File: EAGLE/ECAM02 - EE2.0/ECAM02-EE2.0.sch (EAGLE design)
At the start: 50 parts, among them J1 MODULAR TOOL, J2 SPI, J3 MOT, J4 FTDI, J5 S4B-PH-SM4, J6 S5B-PH-SM, J7 RINGLIGHT, Q2 16MHz, U1 SP3485, U2 ATMEGA238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

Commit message: Component placement begun
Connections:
- removed net O_OUT: U2.PD2
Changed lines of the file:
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@@
-</segment>
-</net>
-<net name="O_OUT" class="0">
-<segment>
-<pinref part="U2" gate="G$1" pin="PD2"/>
-<wire x1="340.36" y1="220.98" x2="347.98" y2="220.98" width="0.1524" layer="91"/>
-<label x="342.9" y="220.98" size="1.778" layer="95" ratio="12"/>
 </segment>
 </net>

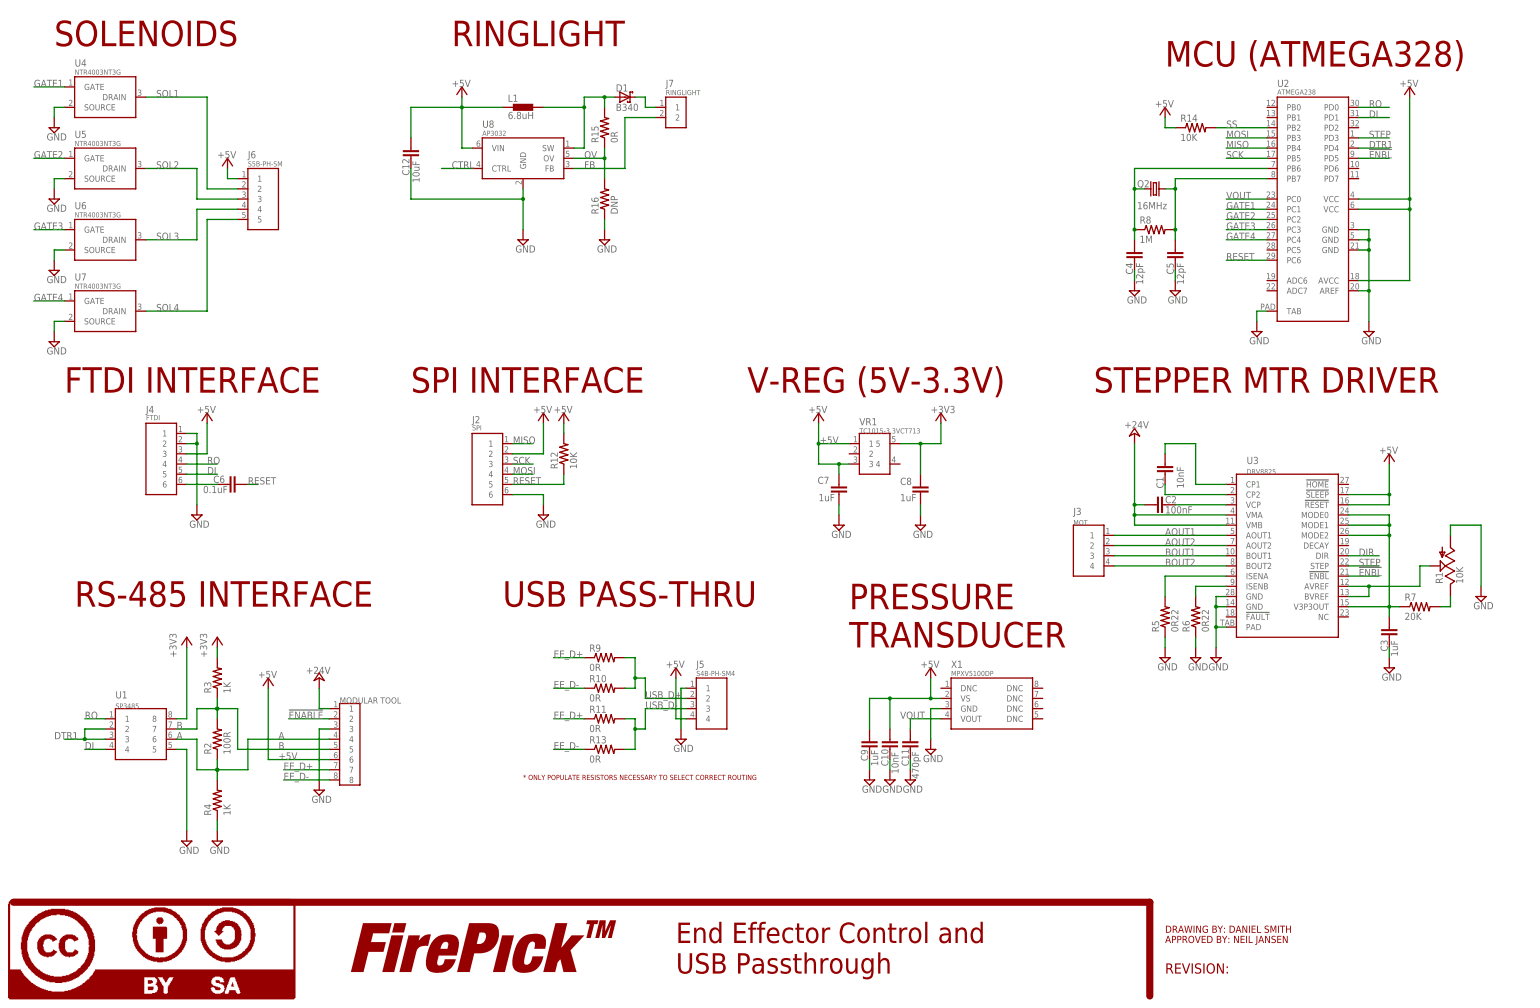
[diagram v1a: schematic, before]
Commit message: Finalized schematics (minus potential LDO regulator) for all boards. Layout partially done for EFD01
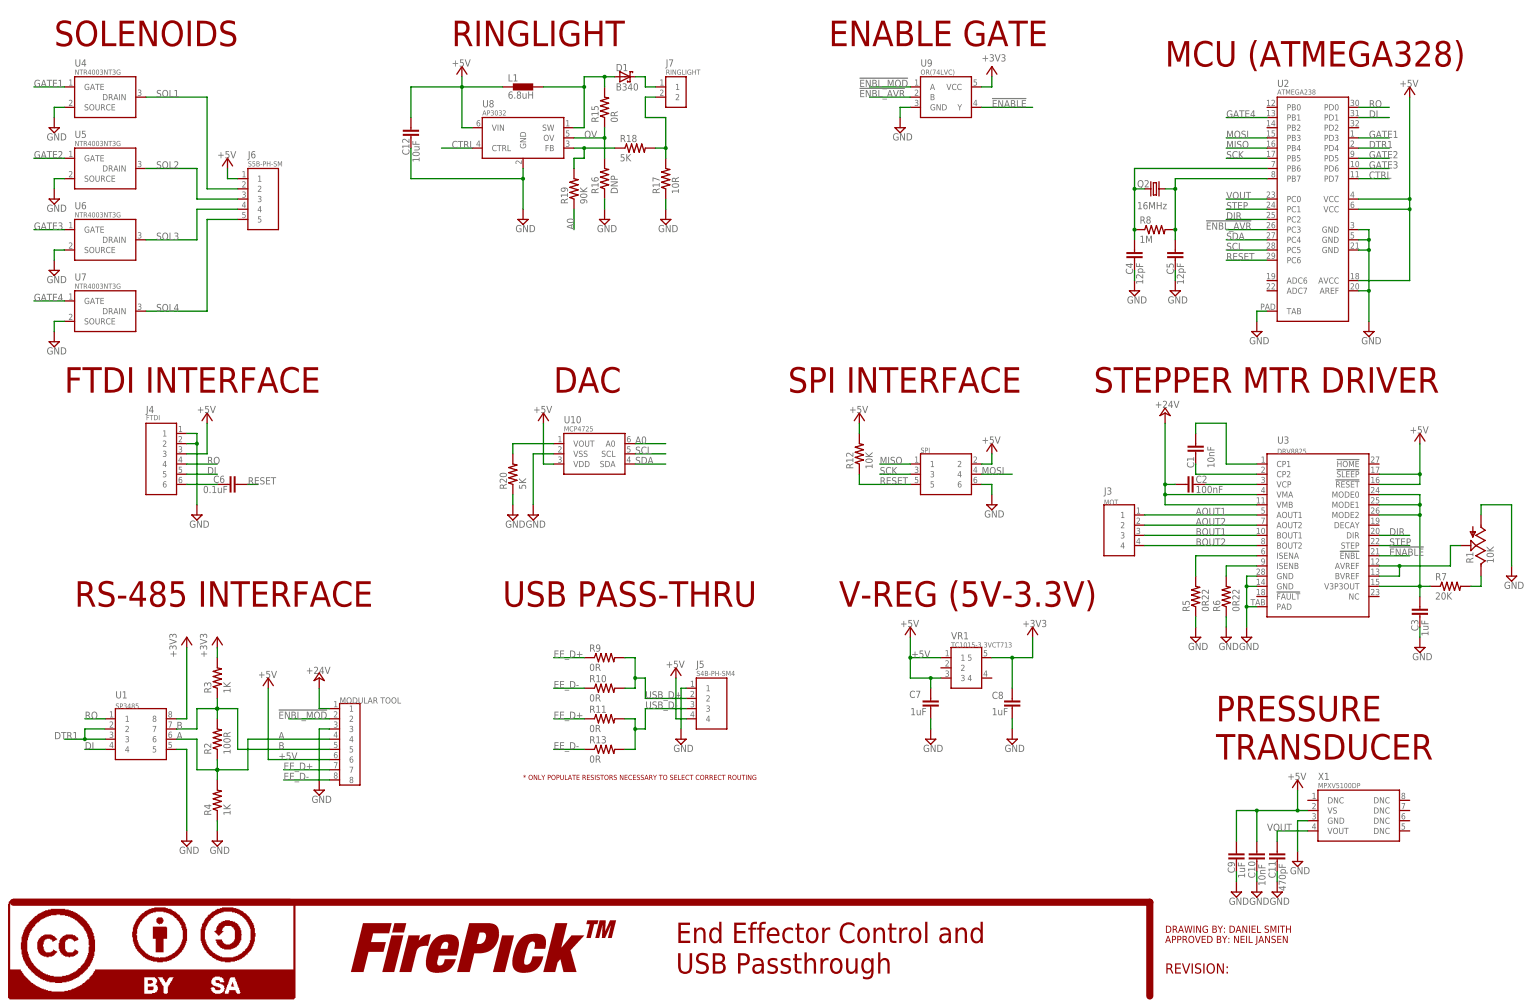
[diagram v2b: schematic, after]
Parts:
- removed R14: 10K, TinWhiskers:CPL-RES-0603-10K-0.1W
- added R17: 10R, TinWhiskers:CPL-RES-0603-10.0-0.1W
- added R18, R20: 5K, TinWhiskers:CPL-RES-0603-5K-0.1W
- added R19: 90K, TinWhiskers:CPL-RES-0603-90K-0.1W
- added U10: MCP4725, TinWhiskers:CPL-DAC-12BIT-SOT23
- added U9: OR(74LVC), TinWhiskers:CPL-IC-LOGIC-OR-1CH-74LVC
- J2: device TinWhiskers:CPL-CON-HEADER-0.1IN-6P-M -> TinWhiskers:CPL-CON-HEADER-0.1IN-2X3P-M; PARTNO 67996-206HLF -> (none)
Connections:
- removed net !ENBL: U2.PD5, U3.!ENBL
- removed net FB: J7.2, U8.FB
- removed net SS: R14.2, U2.PB2
- new net !ENBL_AVR: U2.PC3, U9.B
- new net !ENBL_MOD: J1.2, U9.A
- new net A0: R19.1, U10.A0
- new net N$10: R20.2, U10.VOUT
- new net N$3: J7.2, R17.2, R18.2
- new net N$4: R18.1, R19.2, U8.FB
- new net SCL: U10.SCL, U2.PC5
- new net SDA: U10.SDA, U2.PC4
- net !ENABLE: now also U3.!ENBL, U9.Y; no longer J1.2
- net +3V3: now also U9.VCC
- net +5V: now also U10.VDD; no longer R14.1
- net CTRL: now also U2.PD7
- net DIR: now also U2.PC2
- net GATE1: now also U2.PD3; no longer U2.PC1
- net GATE2: now also U2.PD5; no longer U2.PC2
- net GATE3: now also U2.PD6; no longer U2.PC3
- net GATE4: now also U2.PB1; no longer U2.PC4
- net GND: now also R17.1, R20.1, U10.VSS, U9.GND
- net STEP: now also U2.PC1; no longer U2.PD3
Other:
- note added: "DAC"
- note added: "ENABLE GATE"
- note added: "SPI"
- moved on the sheet: C1, C10, C11, C12, C2, C3, C7, C8, C9, D1, J3, J7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

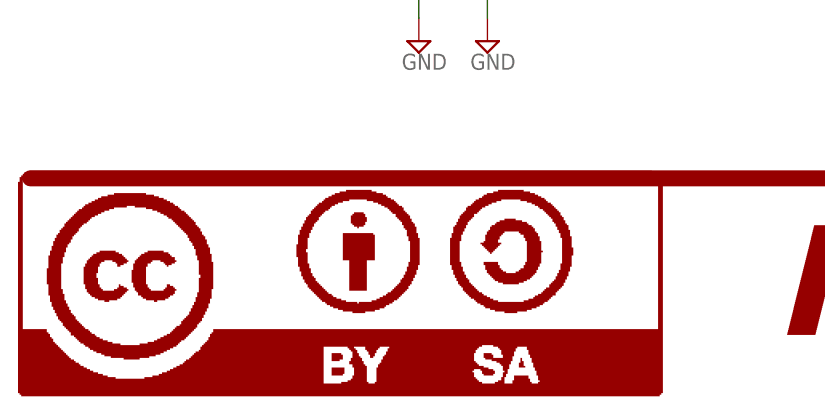
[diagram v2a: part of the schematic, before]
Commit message: Routed all boards. EFP01 has a serious problem with spacing. Even on minimum allowable there are 300 DRC errors.
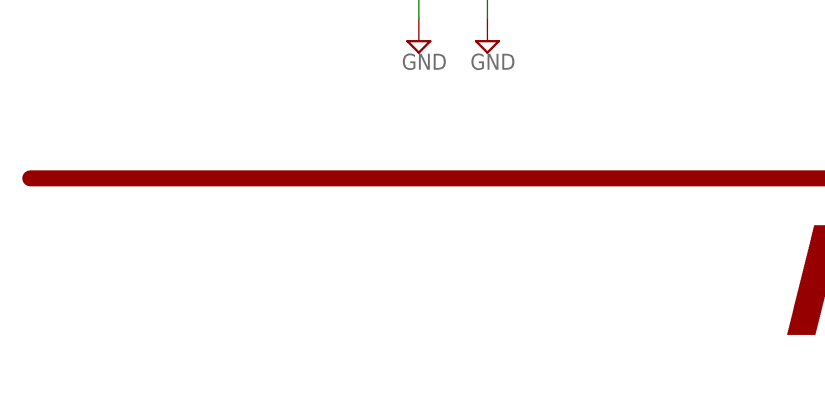
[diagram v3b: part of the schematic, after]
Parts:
- removed LOGO1: LOGO-CC-BY-SALARGE, FirePick:LOGO-CC-BY-SALARGE
- J1: device TinWhiskers:CPL-CON-JST-2.0MM-8P-M-RA -> TinWhiskers:CPL-CON-JST-2.0MM-8P-SMT-VRT
- J3: device TinWhiskers:CPL-CON-JST-2.0MM-4P-M-RA -> TinWhiskers:CPL-CON-HEADER-0.1IN-4P-M
- J4: device TinWhiskers:CPL-CON-JST-2.0MM-6P-M-RA -> TinWhiskers:CPL-CON-JST-2.0MM-6P-SMT-VRT
- J5: device TinWhiskers:CPL-CON-JST-2.0MM-4P-M-SMT-RA -> TinWhiskers:CPL-CON-JST-2.0MM-4P-M-SMT-VRT
- J6: device TinWhiskers:CPL-CON-JST-2.0MM-5P-M-SMT-RA -> TinWhiskers:CPL-CON-JST-2.0MM-5P-SMT-VRT
- J7: device TinWhiskers:CPL-CON-JST-2.0MM-2P-M-SMT-RA -> TinWhiskers:CPL-CON-JST-2.0MM-2P-M-SMT-VRT
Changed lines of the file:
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@@
 <parts>
 <part name="FRAME1" library="TinWhiskers" deviceset="A3L-LOC" device=""/>
-<part name="LOGO1" library="FirePick" deviceset="LOGO-CC-BY-SA" device="LARGE"/>
 <part name="LOGO2" library="FirePick" deviceset="LOGO-FIREPICK" device="LARGE"/>
 <part name="U1" library="TinWhiskers" deviceset="SP3485" device="">
@@
 <part name="P+3" library="supply1" deviceset="+5V" device=""/>
 <part name="+3V1" library="supply1" deviceset="+3V3" device=""/>
-<part name="J4" library="TinWhiskers" deviceset="CPL-CON-JST-2.0MM-6P-M-RA" device="" value="FTDI">
+<part name="J4" library="TinWhiskers" deviceset="CPL-CON-JST-2.0MM-6P-SMT-VRT" device="" value="FTDI">
 <attribute name="PARTNO" value="S6B-PH-SM4-TB(LF)(SN)"/>
 </part>
@@
 </part>
 <part name="SUPPLY8" library="TinWhiskers" deviceset="GND" device=""/>
-<part name="J3" library="TinWhiskers" deviceset="CPL-CON-JST-2.0MM-4P-M-RA" device="" value="MOT">
+<part name="J3" library="TinWhiskers" deviceset="CPL-CON-HEADER-0.1IN-4P-M" device="" value="MOT">
 <attribute name="PARTNO" value="S4B-PH-SM4-TB(LF)(SN)"/>
 </part>
 <part name="SUPPLY13" library="TinWhiskers" deviceset="GND" device=""/>
-<part name="J1" library="TinWhiskers" deviceset="CPL-CON-JST-2.0MM-8P-M-RA" device="" value="MODULAR TOOL">
+<part name="J1" library="TinWhiskers" deviceset="CPL-CON-JST-2.0MM-8P-SMT-VRT" device="" value="MODULAR TOOL">
 <attribute name="PARTNO" value="S8B-PH-SM4-TB(LF)(SN)"/>
 </part>
-<part name="J5" library="TinWhiskers" deviceset="CPL-CON-JST-2.0MM-4P-M-SMT-RA" device="" value="S4B-PH-SM4">
+<part name="J5" library="TinWhiskers" deviceset="CPL-CON-JST-2.0MM-4P-M-SMT-VRT" device="" value="S4B-PH-SM4">
 <attribute name="PARTNO" value="S4B-PH-SM4-TB(LF)(SN)"/>
 </part>
@@
 <part name="SUPPLY24" library="TinWhiskers" deviceset="GND" device=""/>
 <part name="SUPPLY25" library="TinWhiskers" deviceset="GND" device=""/>
-<part name="J6" library="TinWhiskers" deviceset="CPL-CON-JST-2.0MM-5P-M-SMT-RA" device="" value="S5B-PH-SM"/>
+<part name="J6" library="TinWhiskers" deviceset="CPL-CON-JST-2.0MM-5P-SMT-VRT" device="" value="S5B-PH-SM"/>
 <part name="P+13" library="supply1" deviceset="+5V" device=""/>
 <part name="D1" library="TinWhiskers" deviceset="CPL-DIO-B340-13-F-SMA" device="" value="B340"/>
@@
 <part name="R16" library="TinWhiskers" deviceset="CPL-RES-0603-0-0.1W" device="" value="DNP"/>
 <part name="SUPPLY26" library="TinWhiskers" deviceset="GND" device=""/>
-<part name="J7" library="TinWhiskers" deviceset="CPL-CON-JST-2.0MM-2P-M-SMT-RA" device="" value="RINGLIGHT"/>
+<part name="J7" library="TinWhiskers" deviceset="CPL-CON-JST-2.0MM-2P-M-SMT-VRT" device="" value="RINGLIGHT"/>
 <part name="U9" library="TinWhiskers" deviceset="CPL-IC-LOGIC-OR-1CH-74LVC" device="" value="OR(74LVC)"/>
 <part name="SUPPLY28" library="TinWhiskers" deviceset="GND" device=""/>
@@
 <instances>
 <instance part="FRAME1" gate="G$1" x="0" y="0"/>
-<instance part="LOGO1" gate="G$1" x="3.81" y="3.81"/>
 <instance part="LOGO2" gate="G$1" x="88.9" y="10.16"/>
 <instance part="U1" gate="G$1" x="33.02" y="68.58" smashed="yes">

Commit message: Updated all boards to include changes for production
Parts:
- added C13, C14, C15, C16: 0.1uF, TinWhiskers:CPL-CAP-X7R-0603-0.1UF-35V
- added C17: 100uF, TinWhiskers:CPL-CAP-ALU-SMD-100UF-50V
- added C18: 10uF, TinWhiskers:CPL-CAP-ALU-6.4MM-10UF-10V
- added U11: NTR4003NT3G, TinWhiskers:CPL-MOSFET-NCH-SOT23
- J3: device TinWhiskers:CPL-CON-HEADER-0.1IN-4P-M -> TinWhiskers:CPL-CON-JST-2.0MM-4P-M-THRU-VRT
- J4: device TinWhiskers:CPL-CON-JST-2.0MM-6P-SMT-VRT -> TinWhiskers:CPL-CON-HEADER-0.1IN-6P-M
- J6: value S5B-PH-SM -> SOL+PUMP; device TinWhiskers:CPL-CON-JST-2.0MM-5P-SMT-VRT -> TinWhiskers:CPL-CON-JST-2.0MM-7P-M-SMT-VRT
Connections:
- new net N$12: J6.7, U11.DRAIN
- new net PUMP: U11.GATE, U2.PD2
- net +24V: now also C17.NEG, J6.1
- net +3V3: now also C14.2, C16.2
- net +5V: now also C13.2, C15.2, C18.NEG, J6.2; no longer J6.1
- net GND: now also C13.1, C14.1, C15.1, C16.1, C17.POS, C18.POS, U11.SOURCE; no longer U2.TAB
- net SOL1: now also J6.3; no longer J6.2
- net SOL2: now also J6.4; no longer J6.3
- net SOL3: now also J6.5; no longer J6.4
- net SOL4: now also J6.6; no longer J6.5

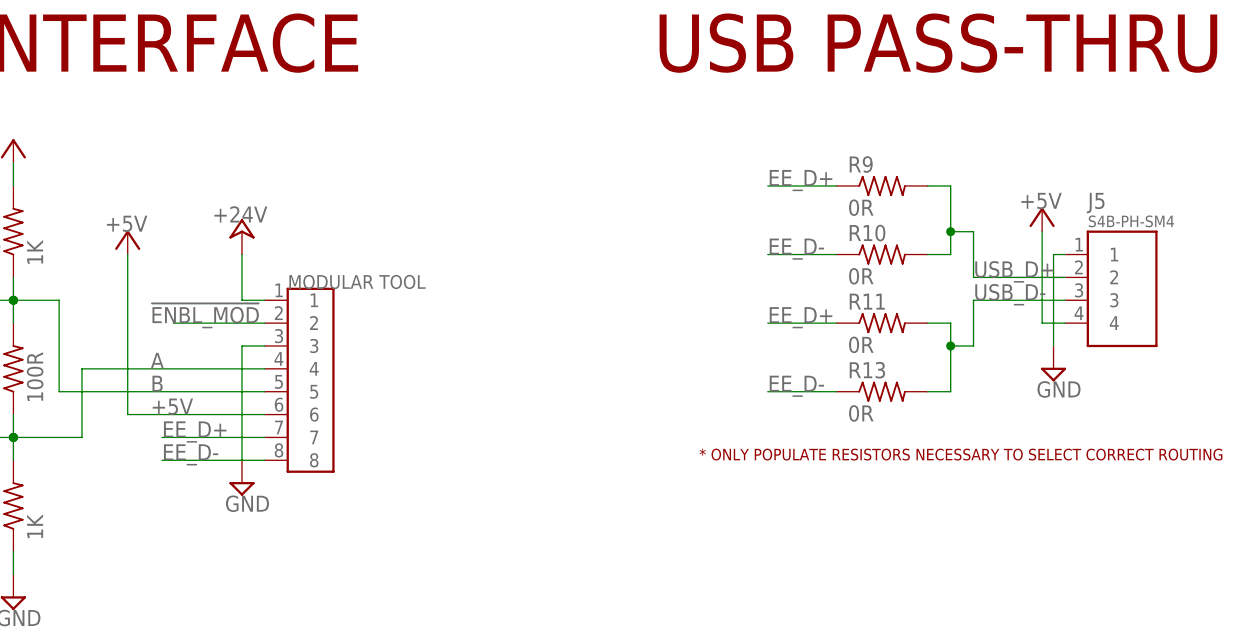
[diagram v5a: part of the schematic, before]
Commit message: Partially-routed diff pairs
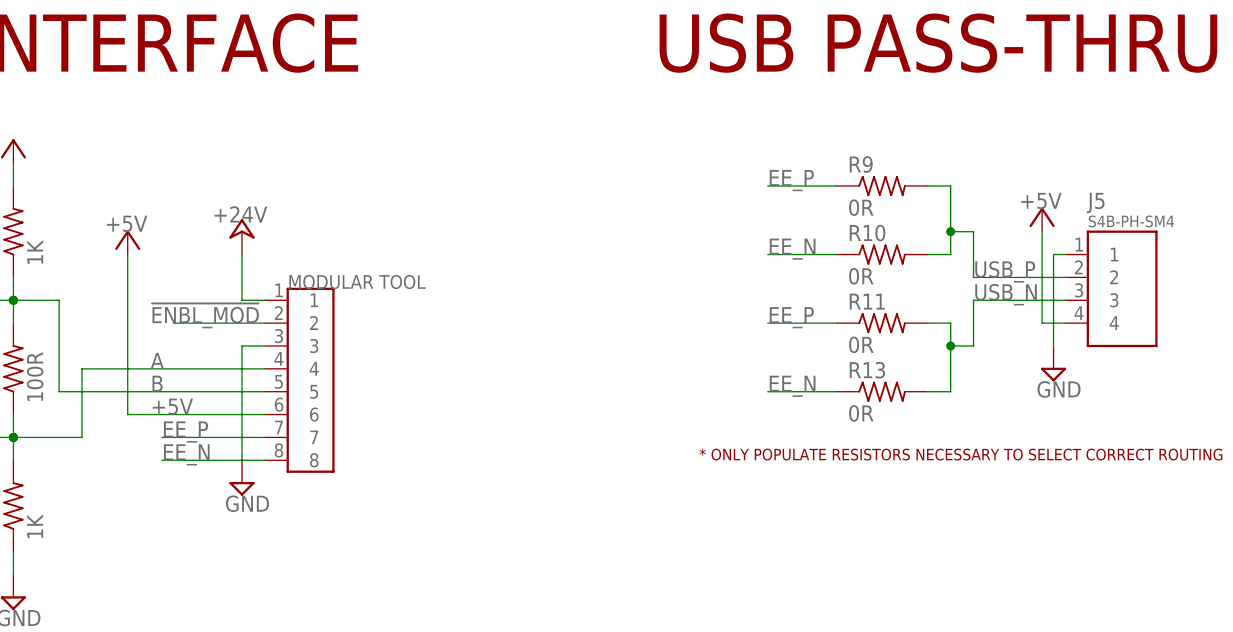
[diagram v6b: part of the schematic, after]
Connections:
- net EE_D+ renamed EE_P
- net EE_D- renamed EE_N
- net USB_D+ renamed USB_P
- net USB_D- renamed USB_N
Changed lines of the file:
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@@
 </segment>
 </net>
-<net name="EE_D+" class="0">
-<segment>
-<pinref part="J1" gate="G$1" pin="7"/>
-<wire x1="83.82" y1="60.96" x2="72.39" y2="60.96" width="0.1524" layer="91"/>
-<label x="72.39" y="60.96" size="1.778" layer="95"/>
-</segment>
-<segment>
-<wire x1="147.32" y1="88.9" x2="139.7" y2="88.9" width="0.1524" layer="91"/>
-<label x="139.7" y="88.9" size="1.778" layer="95" ratio="12"/>
-<pinref part="R9" gate="R$1" pin="1"/>
-</segment>
-<segment>
-<pinref part="R11" gate="R$1" pin="1"/>
-<wire x1="147.32" y1="73.66" x2="139.7" y2="73.66" width="0.1524" layer="91"/>
-<label x="139.7" y="73.66" size="1.778" layer="95" ratio="12"/>
-</segment>
-</net>
-<net name="EE_D-" class="0">
-<segment>
-<pinref part="J1" gate="G$1" pin="8"/>
-<wire x1="83.82" y1="58.42" x2="72.39" y2="58.42" width="0.1524" layer="91"/>
-<label x="72.39" y="58.42" size="1.778" layer="95"/>
-</segment>
-<segment>
-<wire x1="147.32" y1="66.04" x2="139.7" y2="66.04" width="0.1524" layer="91"/>
-<label x="139.7" y="66.04" size="1.778" layer="95" ratio="12"/>
-<pinref part="R13" gate="R$1" pin="1"/>
-</segment>
-<segment>
-<pinref part="R10" gate="R$1" pin="1"/>
-<wire x1="147.32" y1="81.28" x2="139.7" y2="81.28" width="0.1524" layer="91"/>
-<label x="139.7" y="81.28" size="1.778" layer="95" ratio="12"/>
-</segment>
-</net>
-<net name="USB_D+" class="0">
+<net name="USB_P" class="0">
 <segment>
 <pinref part="J5" gate="G$1" pin="2"/>
@@
 </segment>
 </net>
-<net name="USB_D-" class="0">
+<net name="USB_N" class="0">
 <segment>
 <pinref part="J5" gate="G$1" pin="3"/>
@@
 </segment>
 </net>
+<net name="EE_P" class="0">
+<segment>
+<pinref part="J1" gate="G$1" pin="7"/>
+<wire x1="83.82" y1="60.96" x2="72.39" y2="60.96" width="0.1524" layer="91"/>
+<label x="72.39" y="60.96" size="1.778" layer="95"/>
+</segment>
+<segment>
+<wire x1="147.32" y1="88.9" x2="139.7" y2="88.9" width="0.1524" layer="91"/>
+<label x="139.7" y="88.9" size="1.778" layer="95" ratio="12"/>
+<pinref part="R9" gate="R$1" pin="1"/>
+</segment>
+<segment>
+<pinref part="R11" gate="R$1" pin="1"/>
+<wire x1="147.32" y1="73.66" x2="139.7" y2="73.66" width="0.1524" layer="91"/>
+<label x="139.7" y="73.66" size="1.778" layer="95" ratio="12"/>
+</segment>
+</net>
+<net name="EE_N" class="0">
+<segment>
+<pinref part="J1" gate="G$1" pin="8"/>
+<wire x1="83.82" y1="58.42" x2="72.39" y2="58.42" width="0.1524" layer="91"/>
+<label x="72.39" y="58.42" size="1.778" layer="95"/>
+</segment>
+<segment>
+<pinref part="R10" gate="R$1" pin="1"/>
+<wire x1="147.32" y1="81.28" x2="139.7" y2="81.28" width="0.1524" layer="91"/>
+<label x="139.7" y="81.28" size="1.778" layer="95" ratio="12"/>
+</segment>
+<segment>
+<wire x1="147.32" y1="66.04" x2="139.7" y2="66.04" width="0.1524" layer="91"/>
+<label x="139.7" y="66.04" size="1.778" layer="95" ratio="12"/>
+<pinref part="R13" gate="R$1" pin="1"/>
+</segment>
+</net>
